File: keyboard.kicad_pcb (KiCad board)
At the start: 4 copper layers, 82 x 96 mm, 75 parts, among them J1 USB_C_Receptacle_USB2.0_16P, J3 Conn_01x10_Pin, Q1 NMOS, SW1 SW_Push, SW10 SW_Push, SW11 RotaryEncoder_Switch, SW2 SW_Push, SW3 SW_Push, SW4 SW_Push, SW5 SW_Push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

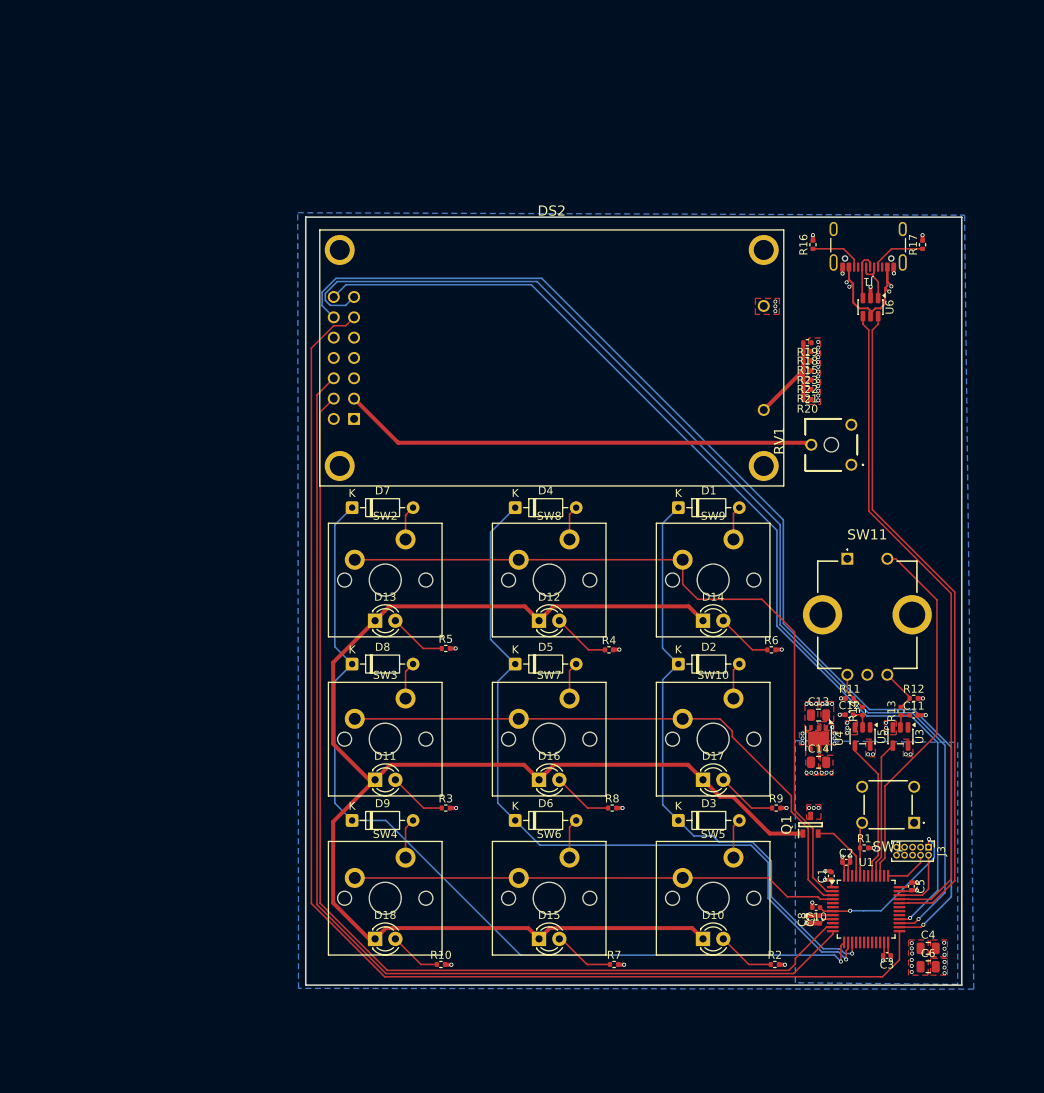
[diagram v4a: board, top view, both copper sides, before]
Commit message: Added 3D models
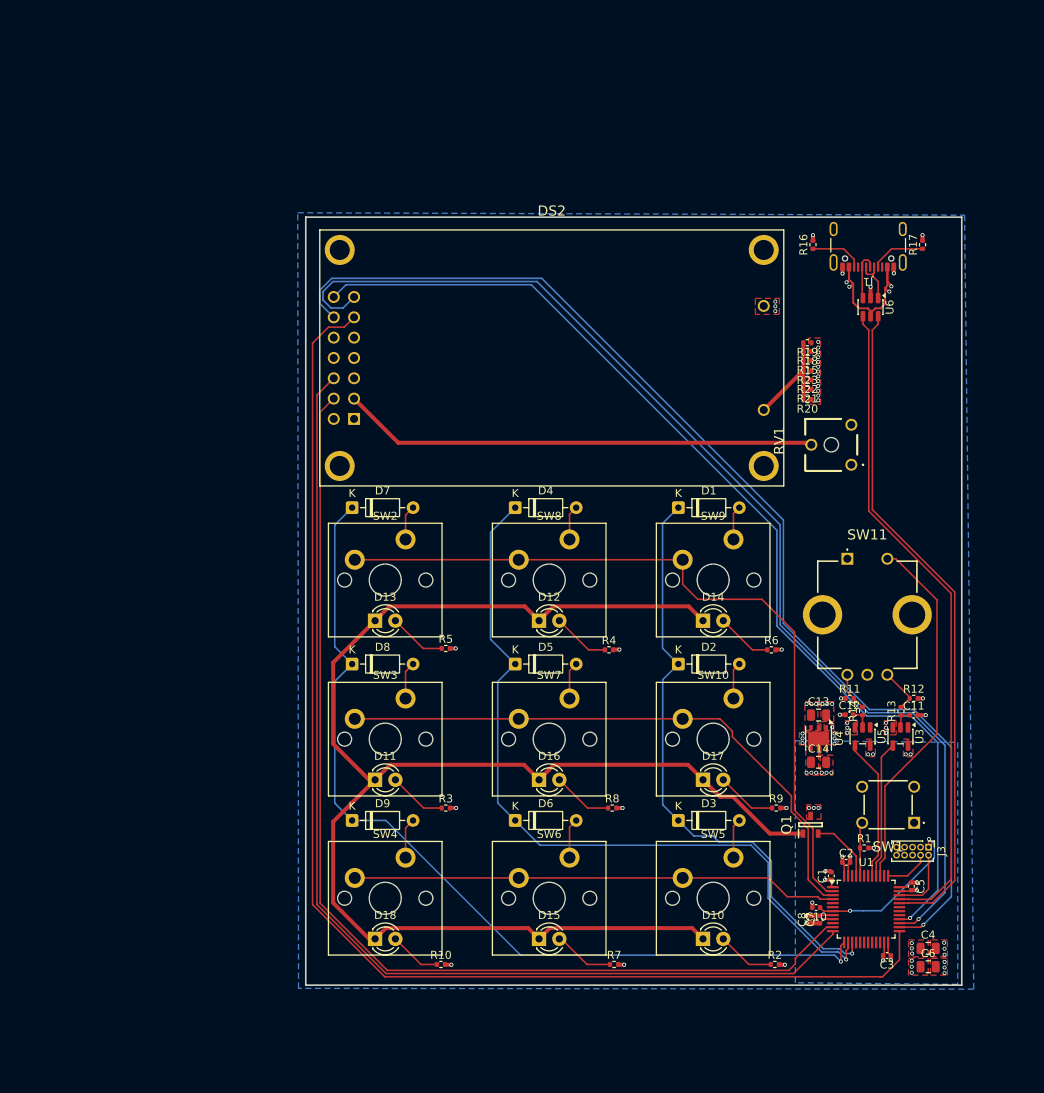
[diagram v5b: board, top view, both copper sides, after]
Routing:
- net /DB6: track 140.3 -> 141.2 mm
- net /DB5: track 141.7 -> 142.3 mm
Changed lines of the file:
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@@
 		)
 		(embedded_fonts no)
-		(model "${KICAD6_3RD_PARTY}/3dmodels/com_github_perigoso_keyswitch-kicad-library/3d-library.3dshapes/SW_Cherry_MX_PCB.wrl"
+		(model "${KIPRJMOD}/library/3dmodels/3d-library.3dshapes/SW_Cherry_MX_PCB.stp"
 			(offset
 				(xyz 0 0 0)
@@
 		)
 		(embedded_fonts no)
-		(model "${KICAD6_3RD_PARTY}/3dmodels/com_github_perigoso_keyswitch-kicad-library/3d-library.3dshapes/SW_Cherry_MX_PCB.wrl"
+		(model "${KIPRJMOD}/library/3dmodels/3d-library.3dshapes/SW_Cherry_MX_PCB.stp"
 			(offset
 				(xyz 0 0 0)
@@
 		)
 		(embedded_fonts no)
-		(model "601030.stp"
+		(model "${KIPRJMOD}/library/LIB_601030/601030/3D/601030.stp"
 			(offset
-				(xyz 2.499999962 2.559999904 5.959999949)
+				(xyz 2.5 2.56 1.96)
 			)
 			(scale
@@
 			)
 			(rotate
-				(xyz 0 0 0)
+				(xyz -0 -0 -0)
 			)
 		)
@@
 		)
 		(embedded_fonts no)
-		(model "${KICAD6_3RD_PARTY}/3dmodels/com_github_perigoso_keyswitch-kicad-library/3d-library.3dshapes/SW_Cherry_MX_PCB.wrl"
+		(model "${KIPRJMOD}/library/3dmodels/3d-library.3dshapes/SW_Cherry_MX_PCB.stp"
 			(offset
 				(xyz 0 0 0)
@@
 		)
 		(embedded_fonts no)
-		(model "NX3020NAK-QR.stp"
+		(model "${KIPRJMOD}/library/LIB_NX3020NAK-QR/NX3020NAK-QR/3D/NX3020NAK-QR.stp"
 			(offset
 				(xyz 0 0 0)
@@
 		)
 		(embedded_fonts no)
-		(model "${KICAD6_3RD_PARTY}/3dmodels/com_github_perigoso_keyswitch-kicad-library/3d-library.3dshapes/SW_Cherry_MX_PCB.wrl"
+		(model "${KIPRJMOD}/library/3dmodels/3d-library.3dshapes/SW_Cherry_MX_PCB.stp"
 			(offset
 				(xyz 0 0 0)
@@
 		)
 		(embedded_fonts no)
-		(model "NHD-0208BZ-FL-YBW.stp"
+		(model "${KIPRJMOD}/LIB_NHD-0208BZ-FL-YBW/NHD-0208BZ-FL-YBW/3D/NHD-0208BZ-FL-YBW.stp"
 			(offset
 				(xyz 0 0 0)
@@
 		)
 		(embedded_fonts no)
-		(model "${KICAD6_3RD_PARTY}/3dmodels/com_github_perigoso_keyswitch-kicad-library/3d-library.3dshapes/SW_Cherry_MX_PCB.wrl"
+		(model "${KIPRJMOD}/library/3dmodels/3d-library.3dshapes/SW_Cherry_MX_PCB.stp"
 			(offset
 				(xyz 0 0 0)
@@
 		)
 		(embedded_fonts no)
-		(model "TS02-66-55-BK-260-LCR-D.stp"
+		(model "${KIPRJMOD}/library/LIB_TS02-66-55-BK-260-LCR-D/TS02-66-55-BK-260-LCR-D/3D/TS02-66-55-BK-260-LCR-D.stp"
 			(offset
-				(xyz 0 0 0)
+				(xyz 3.25 -2.25 0)
 			)
 			(scale
@@
 			)
 			(rotate
-				(xyz 0 0 0)
+				(xyz -90 -0 -0)
 			)
 		)
@@
 		)
 		(embedded_fonts no)
-		(model "${KICAD6_3RD_PARTY}/3dmodels/com_github_perigoso_keyswitch-kicad-library/3d-library.3dshapes/SW_Cherry_MX_PCB.wrl"
+		(model "${KIPRJMOD}/library/3dmodels/3d-library.3dshapes/SW_Cherry_MX_PCB.stp"
 			(offset
 				(xyz 0 0 0)
@@
 		)
 		(embedded_fonts no)
-		(model "${KICAD6_3RD_PARTY}/3dmodels/com_github_perigoso_keyswitch-kicad-library/3d-library.3dshapes/SW_Cherry_MX_PCB.wrl"
+		(model "${KIPRJMOD}/library/3dmodels/3d-library.3dshapes/SW_Cherry_MX_PCB.stp"
 			(offset
 				(xyz 0 0 0)
@@
 		)
 		(embedded_fonts no)
-		(model "${KICAD6_3RD_PARTY}/3dmodels/com_github_perigoso_keyswitch-kicad-library/3d-library.3dshapes/SW_Cherry_MX_PCB.wrl"
+		(model "${KIPRJMOD}/library/3dmodels/3d-library.3dshapes/SW_Cherry_MX_PCB.stp"
 			(offset
 				(xyz 0 0 0)
@@
 		)
 		(embedded_fonts no)
-		(model "${KICAD6_3RD_PARTY}/3dmodels/com_github_perigoso_keyswitch-kicad-library/3d-library.3dshapes/SW_Cherry_MX_PCB.wrl"
+		(model "${KIPRJMOD}/library/3dmodels/3d-library.3dshapes/SW_Cherry_MX_PCB.stp"
 			(offset
 				(xyz 0 0 0)
@@
 		)
 		(embedded_fonts no)
-		(model "PEC12R-3220F-S0024.stp"
+		(model "${KIPRJMOD}/library/LIB_PEC12R-3220F-S0024/PEC12R-3220F-S0024/3D/PEC12R-3220F-S0024.stp"
 			(offset
 				(xyz 2.380000079 -7.050000085 5.059999867)
@@
 	)
 	(via
-		(at 194.55 136.4)
+		(at 194.55 136.5)
 		(size 0.5)
 		(drill 0.3)
@@
 	)
 	(via
-		(at 194.55 137.15)
+		(at 194.55 137.25)
 		(size 0.5)
 		(drill 0.3)
@@
 	)
 	(via
-		(at 194.55 137.9)
+		(at 194.55 138)
 		(size 0.5)
 		(drill 0.3)
@@
 	)
 	(segment
-		(start 119.5 129.3387)
-		(end 119.5 59.923661)
+		(start 190.639232 138.5)
+		(end 190.637232 138.502)
 		(width 0.2)
 		(layer "F.Cu")
@@
 	)
 	(segment
-		(start 123.789 57.121)
+		(start 123.61 57.3)
 		(end 124.84 56.07)
 		(width 0.2)
@@
 	)
 	(segment
-		(start 190.639232 138.5)
-		(end 190.637232 138.502)
+		(start 190.9 138.5)
+		(end 190.639232 138.5)
 		(width 0.2)
 		(layer "F.Cu")
@@
 	)
 	(segment
-		(start 190.9 138.5)
-		(end 190.639232 138.5)
+		(start 119.65 59.3)
+		(end 121.65 57.3)
 		(width 0.2)
 		(layer "F.Cu")
@@
 	)
 	(segment
-		(start 190.637232 138.502)
-		(end 128.6633 138.502)
+		(start 128.6633 138.502)
+		(end 119.65 129.4887)
 		(width 0.2)
 		(layer "F.Cu")
@@
 	)
 	(segment
-		(start 193.1 132.8875)
-		(end 193.0125 132.8)
+		(start 190.637232 138.502)
+		(end 128.6633 138.502)
 		(width 0.2)
 		(layer "F.Cu")
@@
 	)
 	(segment
-		(start 128.6633 138.502)
-		(end 119.5 129.3387)
+		(start 121.65 57.3)
+		(end 123.61 57.3)
 		(width 0.2)
 		(layer "F.Cu")
@@
 	)
 	(segment
-		(start 193.0125 136.3875)
-		(end 190.9 138.5)
+		(start 193.1 132.8875)
+		(end 193.0125 132.8)
 		(width 0.2)
 		(layer "F.Cu")
@@
 	)
 	(segment
-		(start 122.302661 57.121)
-		(end 123.789 57.121)
+		(start 119.65 129.4887)
+		(end 119.65 59.3)
 		(width 0.2)
 		(layer "F.Cu")
@@
 	)
 	(segment
-		(start 119.5 59.923661)
-		(end 122.302661 57.121)
+		(start 193.0125 136.3875)
+		(end 190.9 138.5)
 		(width 0.2)
 		(layer "F.Cu")
@@
 	)
 	(segment
-		(start 178.5 94.338568)
-		(end 189.261432 105.1)
+		(start 122.052 51.198)
+		(end 148.298 51.198)
 		(width 0.2)
 		(layer "B.Cu")
@@
 	)
 	(segment
-		(start 199.5 109.8)
-		(end 199.5 128.5)
+		(start 120.55 52.7)
+		(end 122.052 51.198)
 		(width 0.2)
 		(layer "B.Cu")
@@
 	)
 	(segment
-		(start 194.8 105.1)
-		(end 199.5 109.8)
+		(start 199.5 128.5)
+		(end 196 132)
 		(width 0.2)
 		(layer "B.Cu")
@@
 	)
 	(segment
-		(start 199.5 128.5)
-		(end 196 132)
+		(start 120.55 54.32)
+		(end 120.55 52.7)
 		(width 0.2)
 		(layer "B.Cu")
@@
 	)
 	(segment
-		(start 148.298 51.198)
-		(end 178.5 81.4)
+		(start 189.261432 105.1)
+		(end 194.8 105.1)
 		(width 0.2)
 		(layer "B.Cu")
@@
 	)
 	(segment
-		(start 122.578561 51.198)
-		(end 148.298 51.198)
+		(start 122.3 56.07)
+		(end 120.55 54.32)
 		(width 0.2)
 		(layer "B.Cu")
@@
 	)
 	(segment
-		(start 120.848 54.618)
-		(end 120.848 52.928561)
+		(start 178.5 94.338568)
+		(end 189.261432 105.1)
 		(width 0.2)
 		(layer "B.Cu")
@@
 	)
 	(segment
-		(start 122.3 56.07)
-		(end 120.848 54.618)
+		(start 148.298 51.198)
+		(end 178.5 81.4)
 		(width 0.2)
 		(layer "B.Cu")
@@
 	)
 	(segment
-		(start 189.261432 105.1)
-		(end 194.8 105.1)
+		(start 199.5 109.8)
+		(end 199.5 128.5)
 		(width 0.2)
 		(layer "B.Cu")
@@
 	)
 	(segment
-		(start 120.848 52.928561)
-		(end 122.578561 51.198)
+		(start 194.8 105.1)
+		(end 199.5 109.8)
 		(width 0.2)
 		(layer "B.Cu")
@@
 	)
 	(segment
-		(start 147.699 51.599)
-		(end 178.099 81.999)
+		(start 120.95 53.9)
+		(end 120.95 52.8671)
 		(width 0.2)
 		(layer "B.Cu")
@@
 	)
 	(segment
-		(start 178.099 94.504668)
-		(end 189.095332 105.501)
+		(start 122.2181 51.599)
+		(end 147.699 51.599)
 		(width 0.2)
 		(layer "B.Cu")
@@
 	)
 	(segment
-		(start 124.84 53.53)
-		(end 123.789 54.581)
+		(start 178.099 81.999)
+		(end 178.099 94.504668)
 		(width 0.2)
 		(layer "B.Cu")
@@
 	)
 	(segment
-		(start 122.744661 51.599)
-		(end 147.699 51.599)
+		(start 198.7 128)
+		(end 195.4 131.3)
 		(width 0.2)
 		(layer "B.Cu")
@@
 	)
 	(segment
-		(start 123.789 54.581)
-		(end 121.864661 54.581)
+		(start 120.95 52.8671)
+		(end 122.2181 51.599)
 		(width 0.2)
 		(layer "B.Cu")
@@
 	)
 	(segment
-		(start 189.095332 105.501)
-		(end 194.6339 105.501)
+		(start 124.84 53.53)
+		(end 123.47 54.9)
 		(width 0.2)
 		(layer "B.Cu")
@@
 	)
 	(segment
-		(start 198.7 128)
-		(end 195.4 131.3)
+		(start 194.6339 105.501)
+		(end 198.7 109.5671)
 		(width 0.2)
 		(layer "B.Cu")
@@
 	)
 	(segment
-		(start 194.6339 105.501)
-		(end 198.7 109.5671)
+		(start 123.47 54.9)
+		(end 121.95 54.9)
 		(width 0.2)
 		(layer "B.Cu")
@@
 	)
 	(segment
-		(start 121.864661 54.581)
-		(end 121.249 53.965339)
+		(start 189.095332 105.501)
+		(end 194.6339 105.501)
 		(width 0.2)
 		(layer "B.Cu")
@@
 	)
 	(segment
-		(start 198.7 109.5671)
-		(end 198.7 128)
+		(start 121.95 54.9)
+		(end 120.95 53.9)
 		(width 0.2)
 		(layer "B.Cu")
@@
 	)
 	(segment
-		(start 178.099 81.999)
-		(end 178.099 94.504668)
+		(start 147.699 51.599)
+		(end 178.099 81.999)
 		(width 0.2)
 		(layer "B.Cu")
@@
 	)
 	(segment
-		(start 121.249 53.094661)
-		(end 122.744661 51.599)
+		(start 178.099 94.504668)
+		(end 189.095332 105.501)
 		(width 0.2)
 		(layer "B.Cu")
@@
 	)
 	(segment
-		(start 121.249 53.965339)
-		(end 121.249 53.094661)
+		(start 198.7 109.5671)
+		(end 198.7 128)
 		(width 0.2)
 		(layer "B.Cu")
@@
 		(polygon
 			(pts
-				(xy 196.6 133.9) (xy 196.6 138.3) (xy 194.15 138.3) (xy 194.15 133.9)
+				(xy 196.6 133.9) (xy 196.6 136) (xy 194.15 136) (xy 194.15 133.9)
+			)
+		)
+	)
+	(zone
+		(net 13)
+		(net_name "+3.3V")
+		(layer "F.Cu")
+		(hatch edge 0.5)
+		(priority 13)
+		(connect_pads yes
+			(clearance 0.5)
+		)
+		(min_thickness 0.25)
+		(filled_areas_thickness no)
+		(fill yes
+			(thermal_gap 0.5)
+			(thermal_bridge_width 0.5)
+		)
+		(polygon
+			(pts
+				(xy 196.6 136.2) (xy 196.6 138.3) (xy 194.15 138.3) (xy 194.15 136.2)
 			)
 		)

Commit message: Added oled footprint
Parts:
- removed DS2: NHD-0208BZ-FL-YBW, NHD:NHD0208BZFLYBW
- removed R15, R18, R19, R20, R21, R22, R23: 330R, Resistor_SMD:R_0402_1005Metric
- removed RV1: 10k, my_footprints:601030
- added U2: ~, oled:Bez_nazwy, F.Cu at (150.1, 60.8)
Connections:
- U1 pad 11: /LCD_RS -> unconnected-(U1-PA1-Pad11)
- U1 pad 12: /LCD_ENABLE -> unconnected-(U1-PA2-Pad12)
- U1 pad 25: /DB4 -> unconnected-(U1-PB12-Pad25)
- U1 pad 26: /DB5 -> /I2C_SCL
- U1 pad 27: /DB6 -> /I2C_SDA
- U1 pad 28: /DB7 -> unconnected-(U1-PB15-Pad28)
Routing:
- net /DB4: track 158.4 -> 0.00 mm
- net /DB5: track 142.3 -> 0.00 mm, vias 1 -> 0
- net /DB6: track 141.2 -> 0.00 mm, vias 1 -> 0
- net /LCD_ENABLE: track 137.1 -> 0.00 mm
- net /LCD_RS: track 134.0 -> 0.00 mm
- net /DB7: track 131.6 -> 0.00 mm, vias 1 -> 0
- net /I2C_SCL: track 0.00 -> 113.9 mm, vias 0 -> 2
- net /I2C_SDA: track 0.00 -> 109.2 mm, vias 0 -> 2
- net Net-(DS2-V0): track 59.6 -> 0.00 mm
- net (no net): track 0.00 -> 16.6 mm
- net /LED+: track 14.1 -> 0.00 mm
- net GND: vias 45 -> 42
- net +5V: vias 31 -> 18
